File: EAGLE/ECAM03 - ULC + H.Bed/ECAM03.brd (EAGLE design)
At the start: 160 x 100 mm, 50 parts, among them J1 MODULAR TOOL, J2 SPI, J3 MOT, J4 FTDI, J5 S4B-PH-SM4, J6 S5B-PH-SM, J7 RINGLIGHT, Q2 16MHz, U1 SP3485, U2 ATMEGA238, U3 DRV8825, U4 NTR4003NT3G, U5 NTR4003NT3G, U6 NTR4003NT3G, U7 NTR4003NT3G, U8 AP3032, X1 MPXV5100DP

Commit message: Component placement begun
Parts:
- removed C1, C10: 10nF, TinWhiskers:C0603
- removed C11: 470pF, TinWhiskers:C0603
- removed C2: 100nF, TinWhiskers:C0603
- removed C3, C7, C8, C9: 1uF, TinWhiskers:C0603
- removed C6: 0.1uF, TinWhiskers:C0603
- removed J6: S5B-PH-SM, TinWhiskers:CONN-JST-PH-2.0MM-5P-SMT-RA
- removed R12, R14: 10K, TinWhiskers:R0603
- removed R6: 0R22, TinWhiskers:R1206
- removed R7: 20K, TinWhiskers:R0603
- removed U6: NTR4003NT3G, TinWhiskers:SOT-23-3
- removed VR1: TC1015-3.3VCT713, TinWhiskers:SOT-23-5
- removed X1: MPXV5100DP, TinWhiskers:8-SMD
- added TB1: T-BLOCK, TinWhiskers:TBLOCK-2-5MM
- J2: value SPI -> FAN1; device TinWhiskers:CON-HDR-6POS-MALE -> TinWhiskers:CON-HDR-3POS-MALE
- J3: value MOT -> FAN2; device TinWhiskers:CONN-JST-PH-2.0MM-4P-SMT-RA -> TinWhiskers:CON-HDR-3POS-MALE
- J4: value FTDI -> FAN3; device TinWhiskers:CONN-JST-PH-2.0MM-6P-SMT-RA -> TinWhiskers:CON-HDR-3POS-MALE
- R1: device TinWhiskers:TC33X-2 -> TinWhiskers:R0603
- R5: value 0R22 -> 5K; device TinWhiskers:R1206 -> TinWhiskers:R0603
- U3: value DRV8825 -> MCP4725; device TinWhiskers:28-HSSOP -> TinWhiskers:SOT-23-6
- U4: value NTR4003NT3G -> MAX31855; device TinWhiskers:SOT-23-3 -> TinWhiskers:SOICN-8
- moved U3 52.1 mm to (-53.3, 57.1)
- moved J4 49.9 mm to (-47.0, 69.8)
- moved U4 49.6 mm to (-58.4, 36.8)
- moved R13 39.5 mm to (-52.1, 61.0)
- moved R15 39.5 mm to (-59.7, 61.0)
- moved U7 35.3 mm to (-41.9, 57.1)
- moved U2 34.3 mm to (-27.9, 6.35)
- moved C4 33.3 mm to (-36.8, 52.1)
- moved C5 33.3 mm to (-41.9, 52.1)
- moved C12 32.1 mm to (-47.0, 52.1)
- moved J7 30.0 mm to (-52.1, 25.4)
- moved LOGO1 29.0 mm to (-44.5, 34.3)
- moved J3 28.5 mm to (-34.3, 69.8)
- moved J5 26.5 mm to (-30.5, 25.4)
- moved R10 26.1 mm to (-36.8, 61.0)
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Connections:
- removed net !ENBL: U2.9, U3.21
- removed net AOUT1: J3.1, U3.5
- removed net AOUT2: J3.2, U3.7
- removed net BOUT1: J3.3, U3.10
- removed net BOUT2: J3.4, U3.8
- removed net DIR: U3.20
- removed net GATE1: U2.24, U4.1
- removed net GATE2: U2.25, U5.1
- removed net GATE3: U2.26, U6.1
- removed net GATE4: U2.27, U7.1
- removed net N$13: C3.2, R7.1, U3.15, U3.24, U3.25, U3.26
- removed net N$14: R1.3, R7.2
- removed net N$15: R1.2, U3.12, U3.13
- removed net N$16: C6.1, J4.6
- removed net N$6: C1.1, U3.2
- removed net N$7: C2.2, U3.3
- removed net N$8: R5.2, U3.6
- removed net N$9: R6.2, U3.9
- removed net SOL1: J6.2, U4.3
- removed net SOL2: J6.3, U5.3
- removed net SOL3: J6.4, U6.3
- removed net SOL4: J6.5, U7.3
- removed net STEP: U2.1, U3.22
- new net A0: U3.6
- new net CPWR: J5.4, U7.3
- new net FAN: U2.9, U5.1
- new net FPWR: J2.2, J3.2, J4.2, U5.3
- new net SCL: U2.28, U3.5
- new net SDA: U2.27, U3.4
- new net SSR: U2.1
- new net T+: TB1.2, U4.3
- new net T-: TB1.1, U4.2
- new net TACH1: J2.3, U2.24
- new net TACH2: J3.3, U2.25
- new net TACH3: J4.3, U2.26
- net +24V: now also J2.1, J3.1, J4.1; no longer C2.1, U3.11, U3.4
- net +3V3: no longer C8.2, VR1.5
- net +5V: now also R1.1, U3.3, U4.4, U7.1; no longer C10.2, C7.2, C9.2, J2.2, J4.3, J5.4, J6.1, R12.2, R14.1, U3.16, U3.17, VR1.1, VR1.3, X1.2
- net DI: no longer J4.5
- net GND: now also U3.2, U4.1; no longer C10.1, C11.1, C3.1, C7.1, C8.1, C9.1, J2.6, J4.1, J4.2, R1.1, R6.1, U3.14, U3.28, U3.TAB, U4.2, U6.2, X1.3
- net MISO: now also U4.7; no longer J2.1
- net MOSI: no longer J2.4
- net N$5: now also R5.2; no longer C1.2
- net RESET: no longer C6.2, J2.5, R12.1
- net RO: no longer J4.4
- net SCK: now also U4.5; no longer J2.3
- net SS: now also R1.2, U4.6; no longer R14.2
- net VOUT: no longer C11.2, X1.4

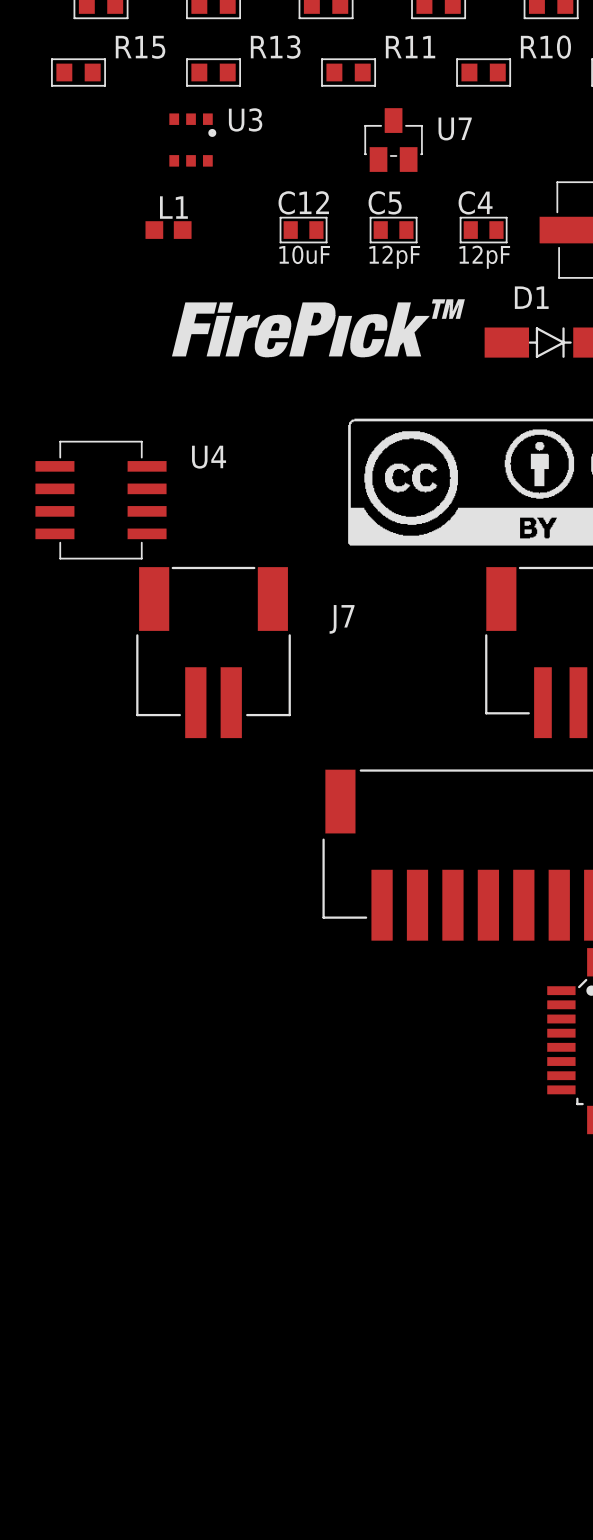
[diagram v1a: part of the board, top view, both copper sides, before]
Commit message: Finalized schematics (minus potential LDO regulator) for all boards. Layout partially done for EFD01
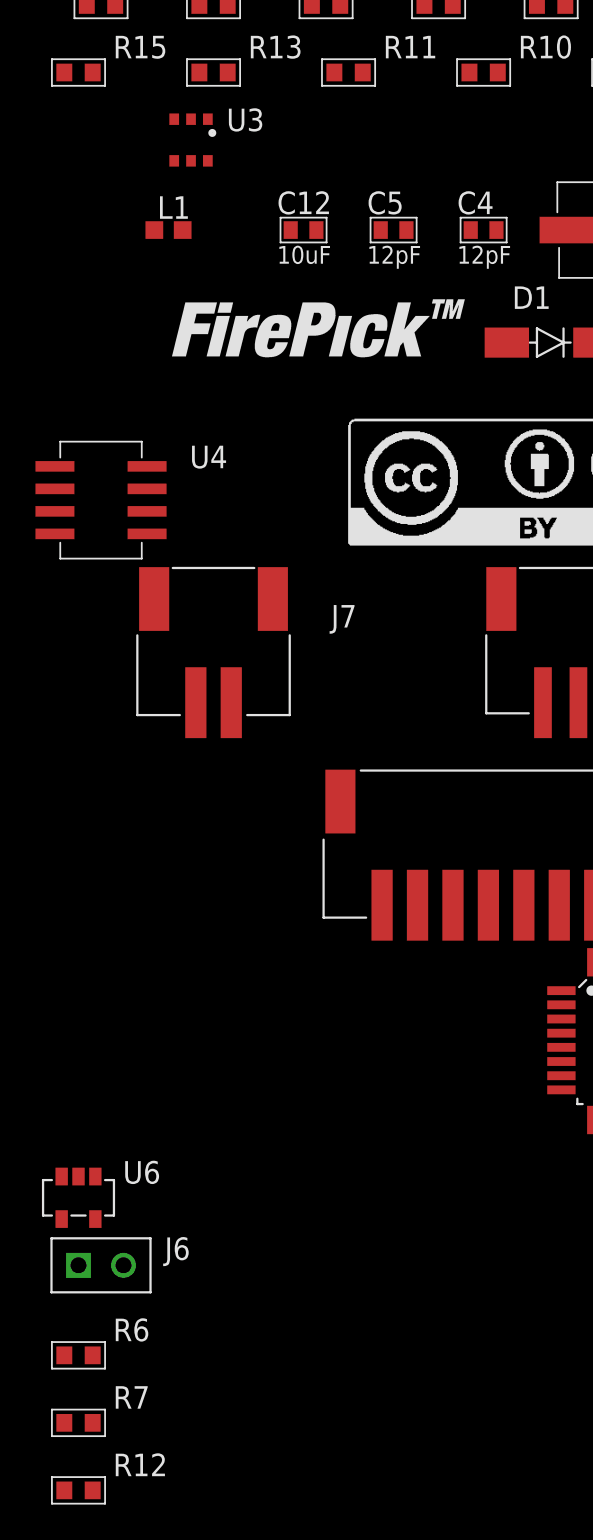
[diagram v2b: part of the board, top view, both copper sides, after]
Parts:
- removed U7: NTR4003NT3G, TinWhiskers:SOT-23-3
- added J6: SSR, TinWhiskers:CON-HDR-2POS-MALE
- added R12: 90K, TinWhiskers:R0603
- added R6: 5K, TinWhiskers:R0603
- added R7: 10R, TinWhiskers:R0603
- added U6: NOR(74LVC), TinWhiskers:SOT-23-5
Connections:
- net FAN renamed FAN_CTL
- removed net !ENABLE: J1.2
- removed net CPWR: J5.4, U7.3
- removed net FB: J7.2, U8.3
- new net !ENBL_AVR: U2.13, U6.2
- new net !ENBL_MOD: J1.2, U6.1
- new net !ENBL_SSR: J6.1, U6.4
- new net N$3: J7.2, R6.2, R7.2
- new net N$4: R12.1, R6.1, U8.3
- net +24V: now also J2.2, J3.2, J4.2; no longer J2.1, J3.1, J4.1
- net +3V3: now also U6.5
- net +5V: now also J5.4; no longer U7.1
- net A0: now also R12.2
- net CTRL: now also U2.11
- net FPWR: now also J2.1, J3.1, J4.1; no longer J2.2, J3.2, J4.2
- net GND: now also J6.2, R7.1, U6.3; no longer U7.2

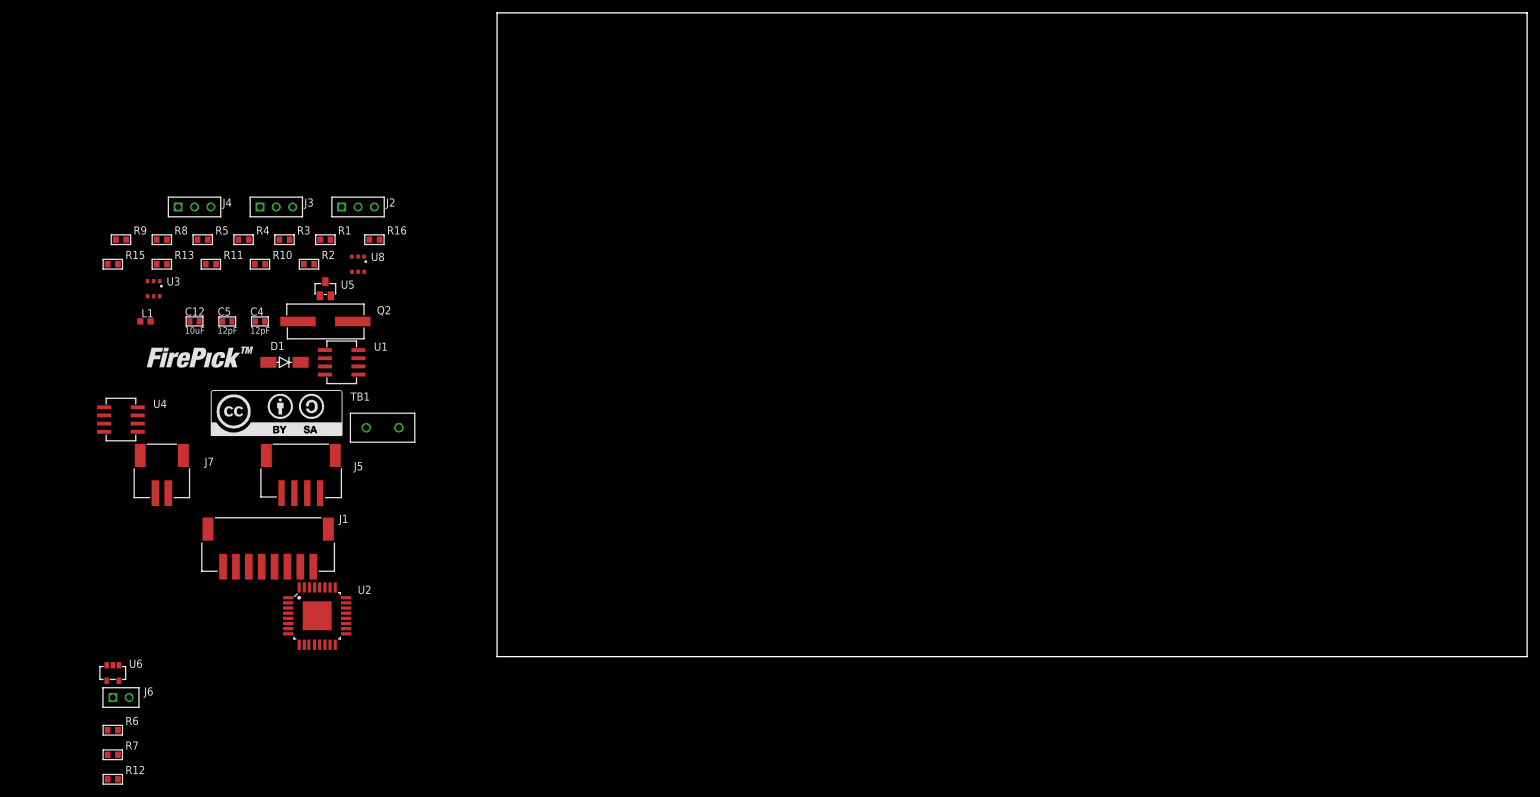
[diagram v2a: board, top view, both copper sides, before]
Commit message: Routed EFD01, ECAM03 boards. Modification needs to be made for hole/keepout in ECAM03. EMC03 X and Y sides routed. Will need to increase some trace widths.
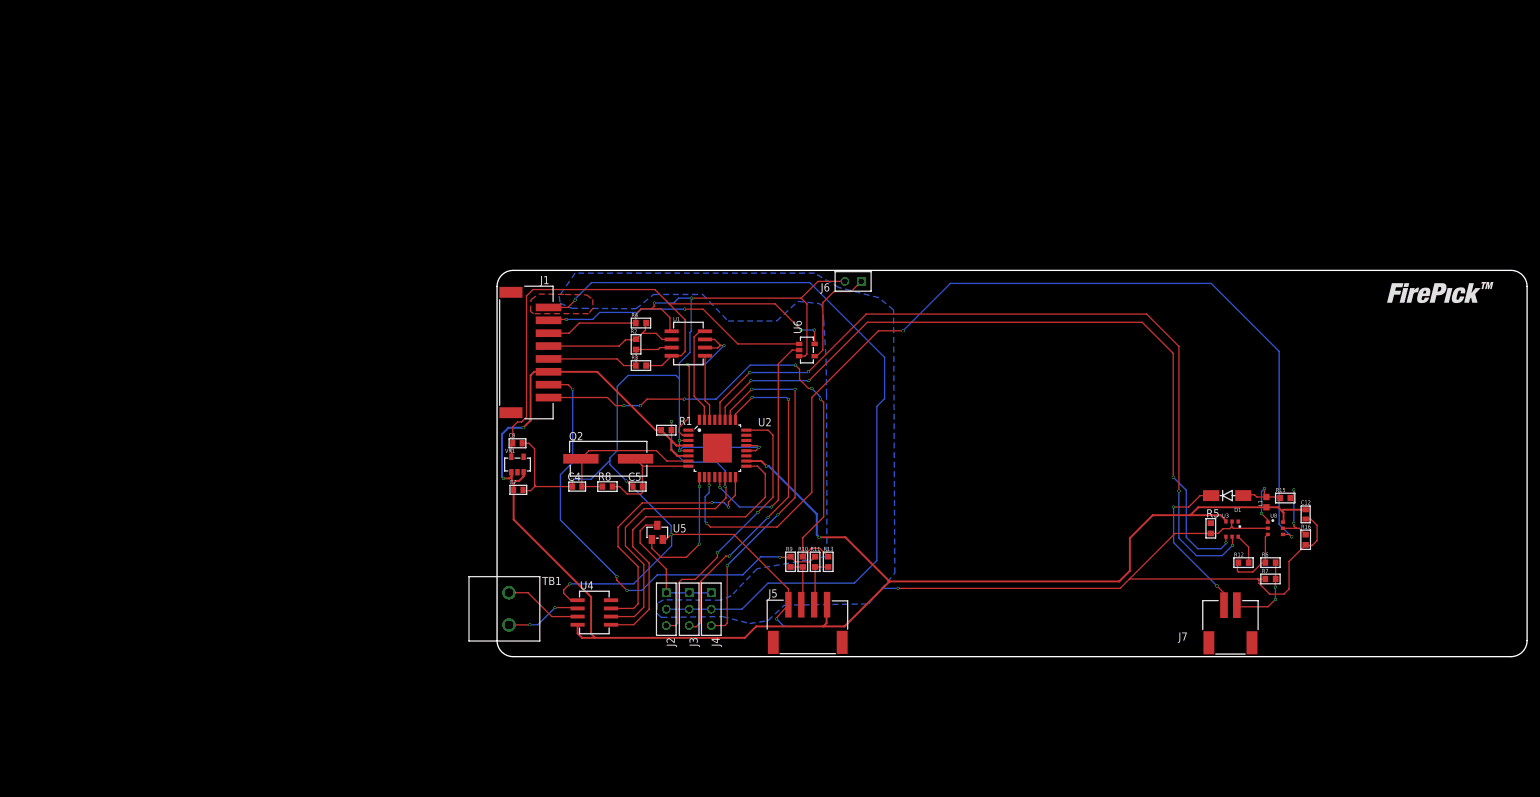
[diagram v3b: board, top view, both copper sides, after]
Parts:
- added C7, C8: 1uF, TinWhiskers:C0603
- added VR1: TC1015-3.3VCT713, TinWhiskers:SOT-23-5
- R2: value 100R -> 120R
- TB1: device TinWhiskers:TBLOCK-2-5MM -> TinWhiskers:TBLOCK-2-5MM-OSTTH020160
- moved LOGO1 204.4 mm to (157.1, 0.13), flipped to the bottom
- moved LOGO2 192.9 mm to (138.0, 53.2)
- moved R15 185.7 mm to (122.4, 24.6), turned to 180 degrees
- moved R7 181.9 mm to (120.1, 12.1)
- moved R6 181.7 mm to (120.1, 14.6)
- moved R12 178.8 mm to (116.0, 14.6)
- moved L1 176.4 mm to (119.5, 24.0), turned to 90 degrees
- moved C12 175.2 mm to (125.6, 22.1), turned to 90 degrees
- moved U3 171.6 mm to (114.2, 19.8)
- moved J7 166.9 mm to (113.9, 8.00), turned to 180 degrees
- moved R5 162.9 mm to (110.9, 19.9), turned to 90 degrees
- moved R16 152.0 mm to (125.6, 18.2), turned to 90 degrees
- moved U8 148.3 mm to (120.9, 19.9), turned to 90 degrees
- moved D1 147.9 mm to (113.4, 25.0), turned to 180 degrees
- moved J6 130.8 mm to (55.3, 58.3), turned to 180 degrees
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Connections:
- net +3V3: now also C8.2, VR1.5
- net +5V: now also C7.2, VR1.1, VR1.3
- net GND: now also C7.1, C8.1
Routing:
- net GND: track 0.00 -> 354.2 mm, vias 0 -> 11
- net +5V: track 0.00 -> 258.3 mm, vias 0 -> 4
- net CTRL: track 0.00 -> 156.5 mm, vias 0 -> 4
- net +24V: track 0.00 -> 126.6 mm, vias 0 -> 1
- net SCL: track 0.00 -> 123.1 mm, vias 0 -> 4
- net SDA: track 0.00 -> 116.8 mm, vias 0 -> 4
- net +3V3: track 0.00 -> 91.6 mm, vias 0 -> 2
- net EE_D-: track 0.00 -> 79.9 mm, vias 0 -> 6
- net EE_D+: track 0.00 -> 72.5 mm, vias 0 -> 4
- net SS: track 0.00 -> 57.9 mm, vias 0 -> 2
- net TACH3: track 0.00 -> 56.2 mm, vias 0 -> 4
- net TACH2: track 0.00 -> 53.0 mm, vias 0 -> 4
- net SCK: track 0.00 -> 50.0 mm
- net TACH1: track 0.00 -> 43.0 mm, vias 0 -> 2
- net !ENBL_MOD: track 0.00 -> 42.0 mm, vias 0 -> 2
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- added copper zone on layer 1, net +24V
- added copper zone on layer 16, net +24V
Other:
- board size 160 x 100 mm -> 160 x 60 mm

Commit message: Updated all boards to include changes for production
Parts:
- J2, J3, J4: device TinWhiskers:CON-HDR-3POS-MALE -> FirePick:CONN-MOLEX-KK-3PIN
- J5: device TinWhiskers:CONN-JST-PH-2.0MM-4P-SMT-RA -> TinWhiskers:CON-JST-PH-2.0MM-4P-SMT-VRT
- J7: device TinWhiskers:CONN-JST-PH-2.0MM-2P-SMT-RA -> TinWhiskers:CON-JST-PH-2.0MM-5P-SMT-VRT
- moved J6 15.6 mm to (41.5, 51.0)
- moved J4 13.0 mm to (45.9, 10.5)
- moved TB1 11.2 mm to (12.4, 11.3), turned to 0 degrees
- moved J3 10.3 mm to (39.7, 10.4)
- moved U4 10.2 mm to (24.7, 10.6)
- moved R10 9.27 mm to (55.3, 19.7)
- moved R11 9.27 mm to (57.2, 19.7)
- moved R13 9.27 mm to (59.3, 19.7)
- moved R9 9.27 mm to (53.4, 19.7)
- moved J2 7.81 mm to (33.5, 10.4)
- moved C7 7.24 mm to (9.30, 21.8)
- moved C8 7.24 mm to (9.17, 29.1)
- moved VR1 7.24 mm to (9.17, 25.8)
- moved J1 7.09 mm to (14.0, 43.5)
- moved D1 6.78 mm to (114.0, 31.8)
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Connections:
- net +5V: now also J7.5
- net GND: now also J7.3
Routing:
- net +24V: track 126.6 -> 0.00 mm, vias 1 -> 4
- net +5V: track 258.3 -> 300.6 mm, vias 4 -> 9
- net +3V3: track 91.6 -> 66.6 mm, vias 2 -> 6
- net EE_D+: track 72.5 -> 94.9 mm, vias 4 -> 2
- net MISO: track 41.8 -> 25.2 mm
- net SCK: track 50.0 -> 36.2 mm, vias 0 -> 2
- net GND: track 354.2 -> 367.1 mm, vias 11 -> 15
- net N$5: track 0.00 -> 11.0 mm, vias 0 -> 2
- net TACH3: track 56.2 -> 47.7 mm
- net TACH1: track 43.0 -> 34.6 mm, vias 2 -> 4
- net FPWR: track 21.4 -> 29.5 mm, vias 0 -> 2
- net TACH2: track 53.0 -> 45.0 mm, vias 4 -> 5
- net EE_D-: track 79.9 -> 71.9 mm, vias 6 -> 5
- net SDA: track 116.8 -> 109.8 mm
- net SCL: track 123.1 -> 116.0 mm
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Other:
- outline, holes or cut-outs redrawn
- board text added: "FAN1"
- board text added: "FAN2"
- board text added: "FAN3"
- board text added: "MILL THIS AREA"
- board text added: "MOD TOOL"
- board text added: "RINGLIGHT"
- board text added: "SSR"
- board text added: "THERM"
- board text added: "USB CAM"

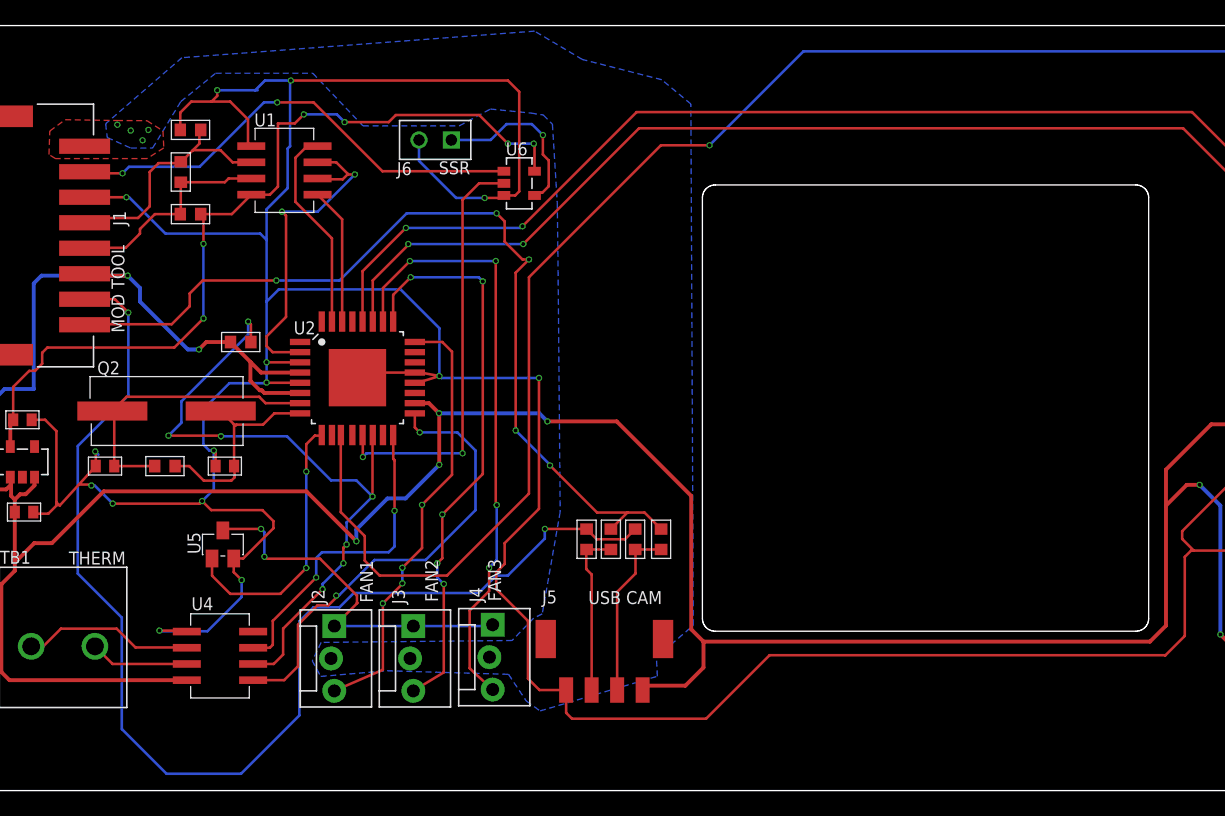
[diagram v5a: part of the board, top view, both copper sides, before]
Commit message: Partially-routed diff pairs
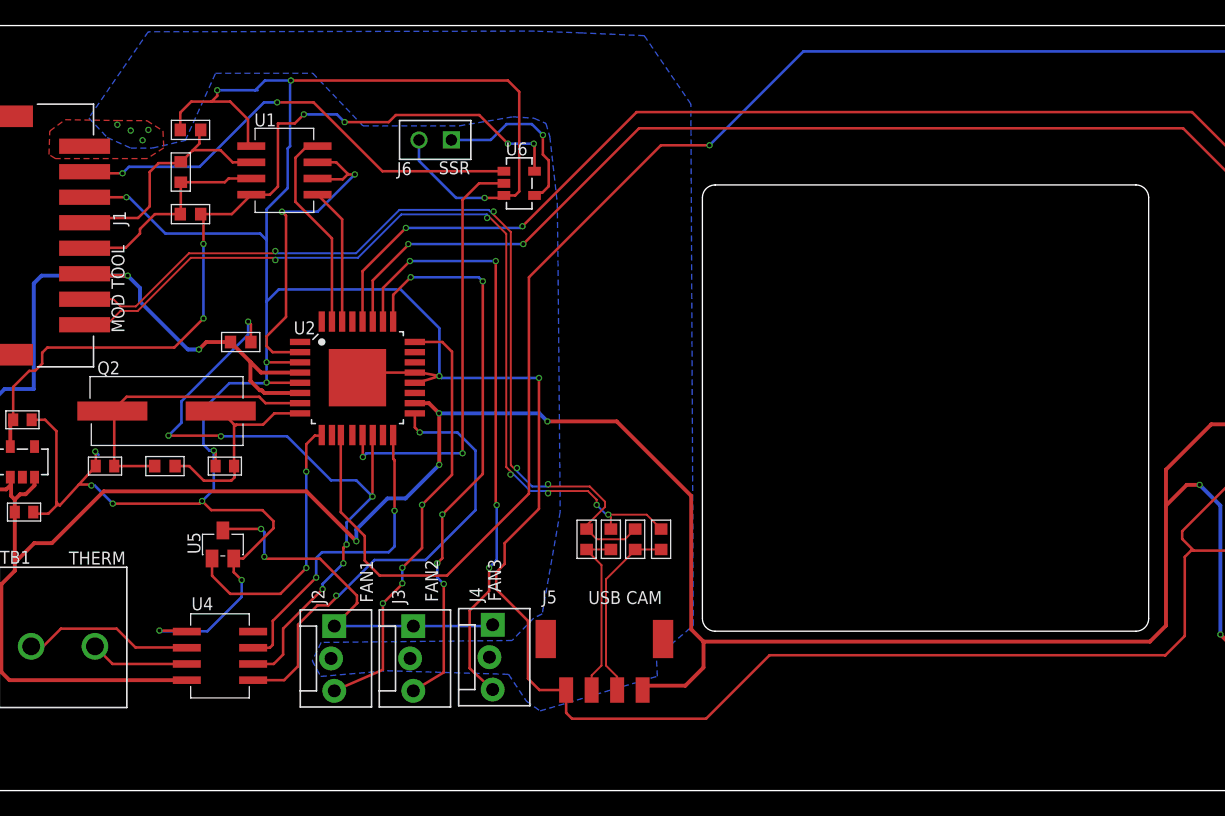
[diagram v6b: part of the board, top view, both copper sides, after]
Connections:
- net EE_D+ renamed ULC_P
- net EE_D- renamed ULC_N
- net USB_D+ renamed USB_P
- net USB_D- renamed USB_N
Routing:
- net ULC_P: track 94.9 -> 73.0 mm, vias 2 -> 4
- net USB_N: track 13.7 -> 14.4 mm
- net ULC_N: track 71.9 -> 72.6 mm, vias 5 -> 6
- net USB_P: track 13.1 -> 13.8 mm
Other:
- outline, holes or cut-outs redrawn
